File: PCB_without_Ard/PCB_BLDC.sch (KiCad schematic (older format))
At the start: 63 parts, among them J1 Power Terminal, J2 Conn_01x03, J3 Conn_01x05, J4 Conn_01x02, J5 Conn_01x04, J6 Conn_01x04, J7 Conn_01x04, J8 Power Terminal, J9 Conn_01x02, Q1 IRF4905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

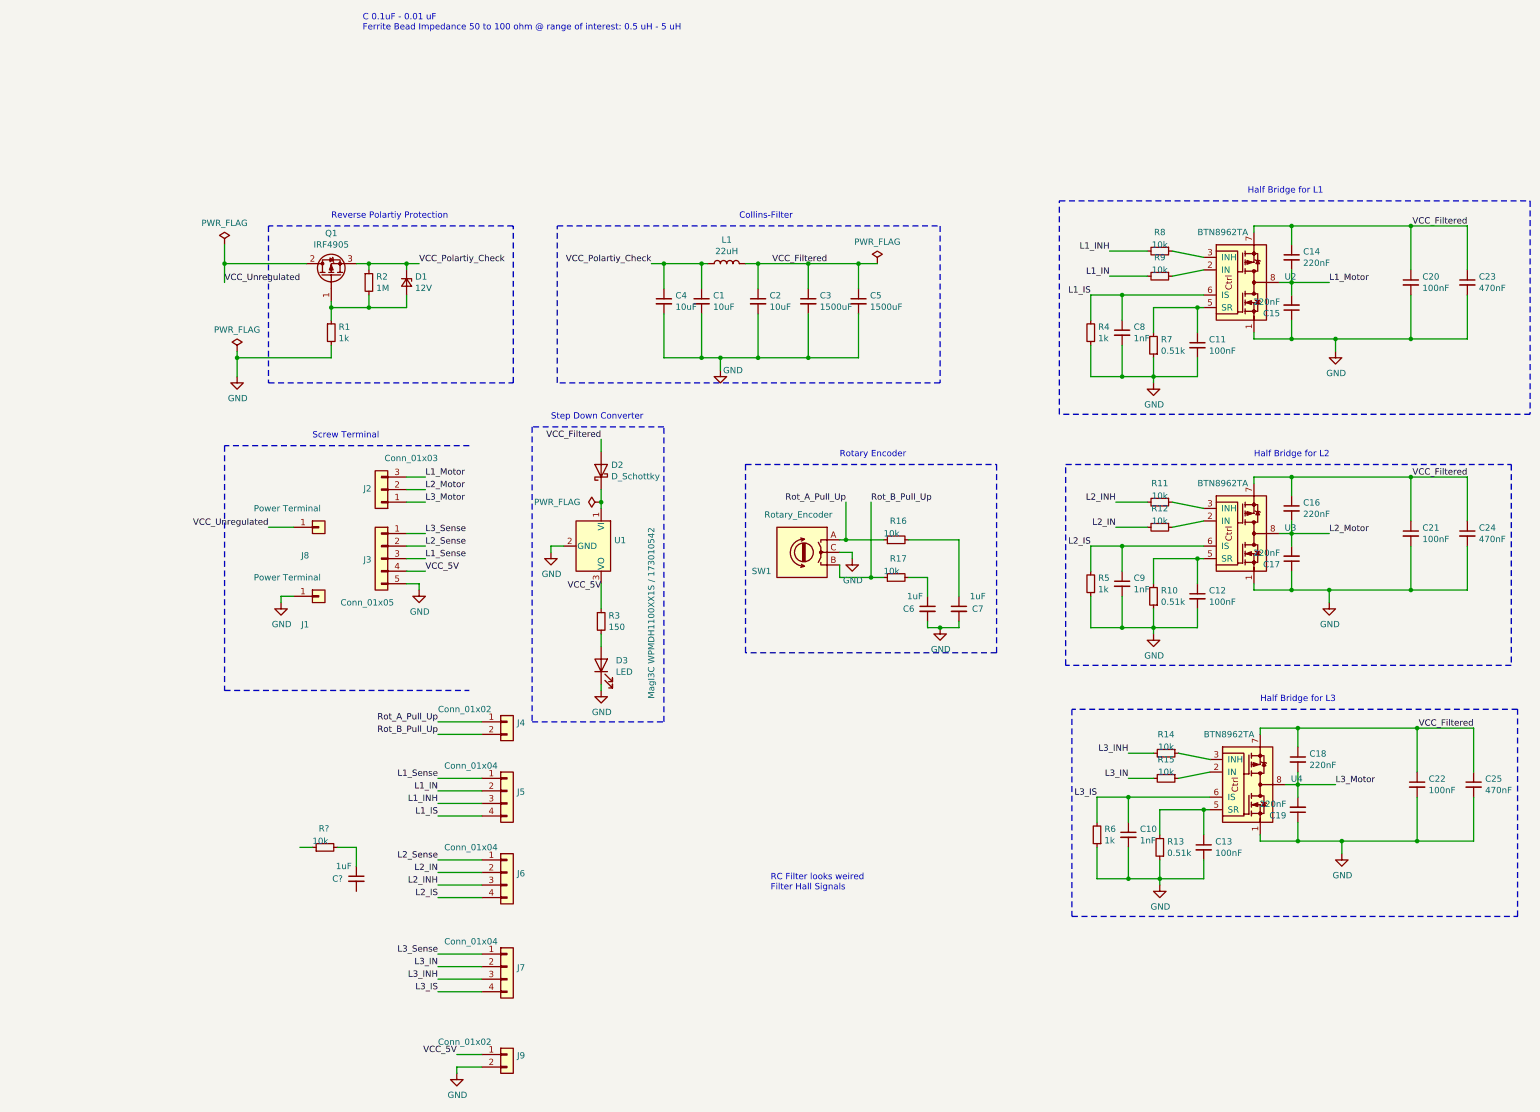
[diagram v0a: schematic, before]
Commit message: Main: Update Schematic, Add Vias, RC-Filt for Hall-Sense
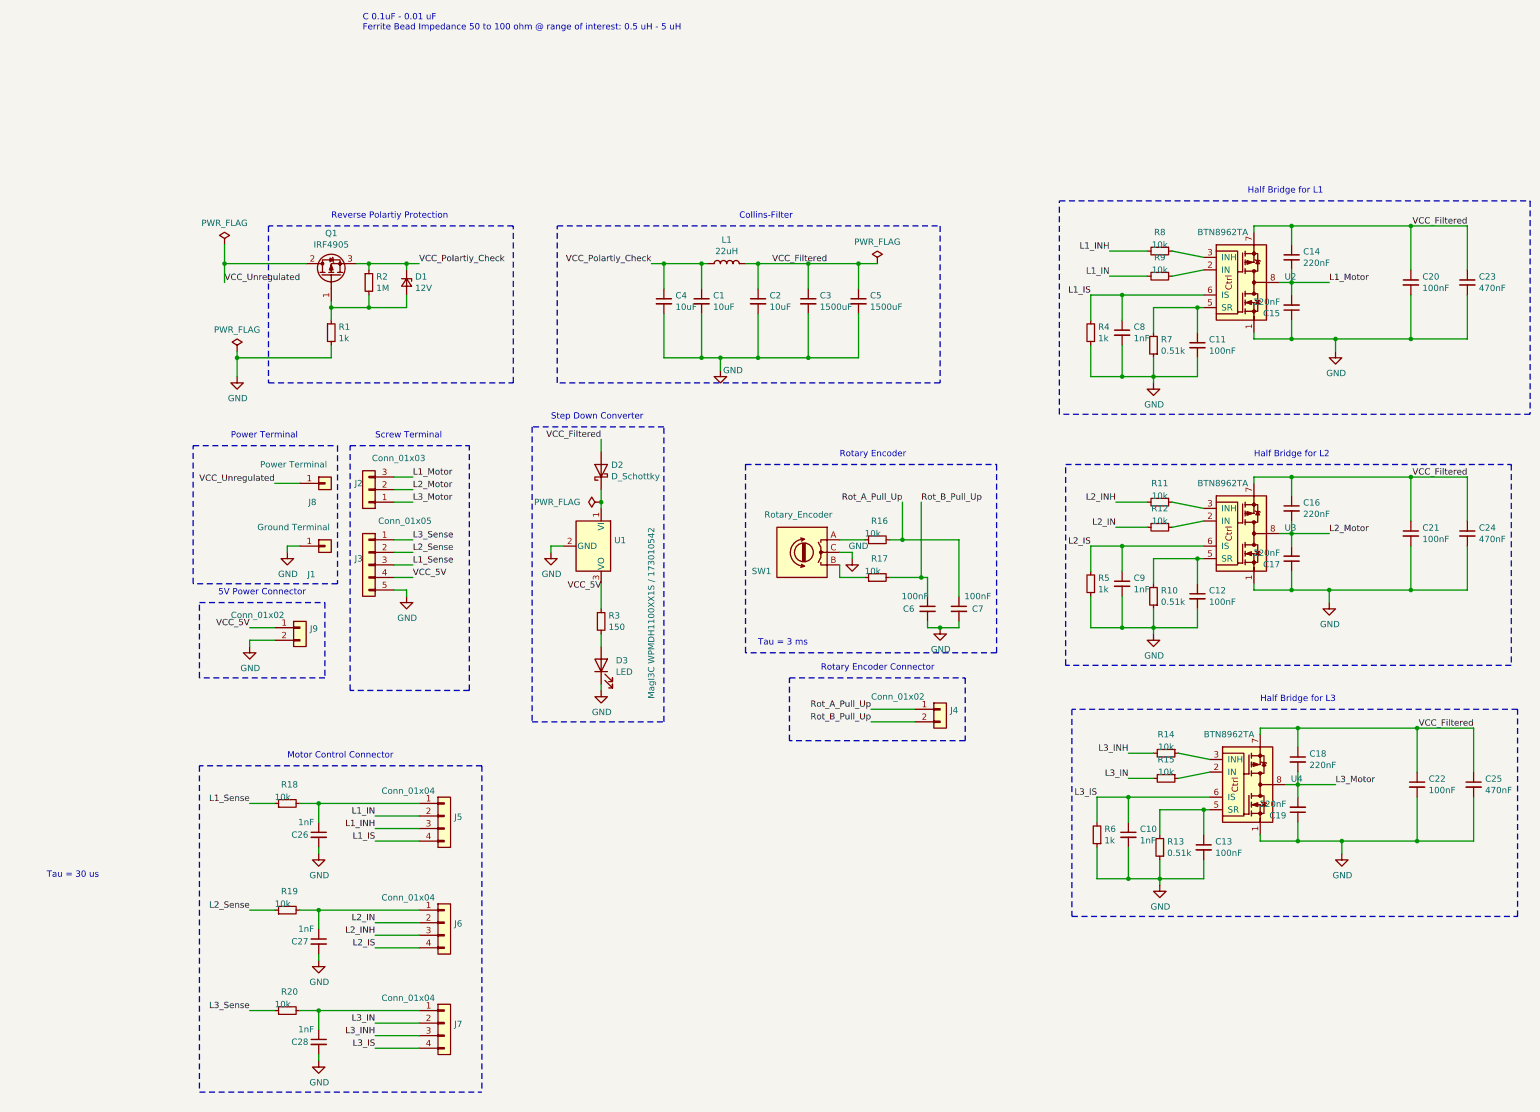
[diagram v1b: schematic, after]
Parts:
- added C27, C28: 1nF, Capacitor_SMD:C_1206_3216Metric_Pad1.33x1.80mm_HandSolder, symbol Device:C_Small
- added R19, R20: 10k, Resistor_SMD:R_1206_3216Metric_Pad1.30x1.75mm_HandSolder, symbol Device:R_Small
- C26: renamed from C?; value 1uF -> 1nF
- C6, C7: value 1uF -> 100nF
- J1: value Power Terminal -> Ground Terminal
- gave numbers to parts that had none: 1
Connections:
- net GND: now also C26.2, C27.2, C28.2
- net L1_Sense: now also R18.1; no longer J5.1 (Pin_1)
- net L2_Sense: now also R19.1; no longer J6.1 (Pin_1)
- net L3_Sense: now also R20.1; no longer J7.1 (Pin_1)
- net Rot_A_Pull_Up: now also C7.1, R16.2; no longer R16.1, SW1.A
- net Rot_B_Pull_Up: now also C6.1, R17.2; no longer R17.1, SW1.B
- net at C26.1, R18.2: now also J5.1 (Pin_1)
- new net: R16.1, SW1.A
- new net: R17.1, SW1.B
- new net: C28.1, J7.1 (Pin_1), R20.2
- new net: C27.1, J6.1 (Pin_1), R19.2
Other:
- note added: "5V Power Connector\n"
- note added: "Motor Control Connector\n"
- note added: "Power Terminal\n"
- note added: "Rotary Encoder Connector\n"
- note added: "Tau = 3 ms"
- note added: "Tau = 30 us"
- note removed: "RC Filter looks weired\nFilter Hall Signals"
- moved on the sheet: C26, J1, J2, J3, J4, J5, J6, J7, J8, J9, R16, R17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

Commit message: PCB: Fixed again Low Pass Filter
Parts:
- added R21, R22, R23, R24, R25: 10k, Resistor_SMD:R_1206_3216Metric_Pad1.30x1.75mm_HandSolder, symbol Device:R_Small
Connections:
- net L1_Sense: now also R21.1
- net L2_Sense: now also R22.1
- net L3_Sense: now also R23.1
- net VCC_5V: now also R21.2, R22.2, R23.2, R24.2, R25.2
- net at R16.1, SW1.A: now also R24.1
- net at R17.1, SW1.B: now also R25.1
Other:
- moved on the sheet: R16, R17
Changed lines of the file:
@@
 Text Label 6300 3050 0    50   ~ 0
 Rot_B_Pull_Up
-Text Label 6150 3050 2    50   ~ 0
+Text Label 6200 2850 0    50   ~ 0
 Rot_A_Pull_Up
 Text Label 10650 850  2    50   ~ 0
@@
 L Device:R_Small R16
 U 1 1 618D47A1
-P 5950 3350
-F 0 "R16" V 6100 3400 50  0000 R CNN
-F 1 "10k" V 6000 3450 50  0000 R CNN
-F 2 "Resistor_SMD:R_1206_3216Metric_Pad1.30x1.75mm_HandSolder" H 5950 3350 50  0001 C CNN
-F 3 "~" H 5950 3350 50  0001 C CNN
-	1    5950 3350
+P 6100 3350
+F 0 "R16" V 6250 3400 50  0000 R CNN
+F 1 "10k" V 6150 3450 50  0000 R CNN
+F 2 "Resistor_SMD:R_1206_3216Metric_Pad1.30x1.75mm_HandSolder" H 6100 3350 50  0001 C CNN
+F 3 "~" H 6100 3350 50  0001 C CNN
+	1    6100 3350
 	0    -1   -1   0
 $EndComp
@@
 L Device:R_Small R17
 U 1 1 618D5B25
-P 5950 3650
-F 0 "R17" V 6100 3700 50  0000 R CNN
-F 1 "10k" V 6000 3750 50  0000 R CNN
-F 2 "Resistor_SMD:R_1206_3216Metric_Pad1.30x1.75mm_HandSolder" H 5950 3650 50  0001 C CNN
-F 3 "~" H 5950 3650 50  0001 C CNN
-	1    5950 3650
+P 6100 3650
+F 0 "R17" V 6250 3700 50  0000 R CNN
+F 1 "10k" V 6150 3750 50  0000 R CNN
+F 2 "Resistor_SMD:R_1206_3216Metric_Pad1.30x1.75mm_HandSolder" H 6100 3650 50  0001 C CNN
+F 3 "~" H 6100 3650 50  0001 C CNN
+	1    6100 3650
 	0    -1   -1   0
 $EndComp
@@
 	5650 3450 5750 3450
 Wire Wire Line
-	6050 3650 6300 3650
+	6200 3650 6300 3650
 Wire Wire Line
 	6350 3650 6350 3800
@@
 	950  4150 950  4200
 Wire Wire Line
-	5650 3650 5850 3650
-Wire Wire Line
-	5650 3350 5850 3350
+	5650 3650 5950 3650
+Wire Wire Line
+	5650 3350 5750 3350
 Wire Wire Line
 	6300 3050 6300 3650
@@
 	6300 3650 6350 3650
 Wire Wire Line
-	6150 3050 6150 3350
-Wire Wire Line
-	6050 3350 6150 3350
-Connection ~ 6150 3350
-Wire Wire Line
-	6150 3350 6600 3350
-Wire Wire Line
 	1350 5450 1500 5450
-Wire Wire Line
-	950  5450 1150 5450
 Wire Wire Line
 	1500 5800 1500 5850
@@
 	1350 7100 1500 7100
 Wire Wire Line
-	950  7100 1150 7100
-Wire Wire Line
 	1500 7450 1500 7500
 $Comp
@@
 Text Label 950  7100 2    50   ~ 0
 L3_Sense
-Wire Wire Line
-	1500 5450 2300 5450
 Connection ~ 1500 5450
-Wire Wire Line
-	1500 7100 2300 7100
 Connection ~ 1500 7100
 Wire Wire Line
 	1350 6300 1500 6300
 Wire Wire Line
-	950  6300 1150 6300
+	950  6300 1050 6300
 Wire Wire Line
 	1500 6650 1500 6700
@@
 	0    -1   -1   0
 $EndComp
-Wire Wire Line
-	1500 6300 2300 6300
 Connection ~ 1500 6300
 Text Notes -250 6050 2    50   ~ 0
@@
 Text Notes 5500 4400 0    50   ~ 0
 Rotary Encoder Connector\n
+$Comp
+L Device:R_Small R24
+U 1 1 618BE346
+P 5750 3100
+F 0 "R24" V 5900 3150 50  0000 R CNN
+F 1 "10k" V 5800 3200 50  0000 R CNN
+F 2 "Resistor_SMD:R_1206_3216Metric_Pad1.30x1.75mm_HandSolder" H 5750 3100 50  0001 C CNN
+F 3 "~" H 5750 3100 50  0001 C CNN
+	1    5750 3100
+	-1   0    0    1
+$EndComp
+Wire Wire Line
+	6200 2850 6200 3350
+Connection ~ 6200 3350
+Wire Wire Line
+	6200 3350 6600 3350
+Wire Wire Line
+	5750 3200 5750 3350
+Connection ~ 5750 3350
+Wire Wire Line
+	5750 3350 6000 3350
+$Comp
+L Device:R_Small R25
+U 1 1 61904EA6
+P 5950 3100
+F 0 "R25" V 6100 3150 50  0000 R CNN
+F 1 "10k" V 6000 3200 50  0000 R CNN
+F 2 "Resistor_SMD:R_1206_3216Metric_Pad1.30x1.75mm_HandSolder" H 5950 3100 50  0001 C CNN
+F 3 "~" H 5950 3100 50  0001 C CNN
+	1    5950 3100
+	-1   0    0    1
+$EndComp
+Wire Wire Line
+	5950 3200 5950 3650
+Connection ~ 5950 3650
+Wire Wire Line
+	5950 3650 6000 3650
+Wire Wire Line
+	5950 3000 5950 2950
+Wire Wire Line
+	5950 2950 5750 2950
+Wire Wire Line
+	5750 2950 5750 3000
+Text Label 5750 2950 2    50   ~ 0
+VCC_5V
+Wire Wire Line
+	1050 6250 1050 6300
+Connection ~ 1050 6300
+Wire Wire Line
+	1050 6300 1150 6300
+Wire Wire Line
+	1500 7100 2300 7100
+Wire Wire Line
+	1050 6800 1050 6850
+Text Label 1050 6800 2    50   ~ 0
+VCC_5V
+$Comp
+L Device:R_Small R23
+U 1 1 61975DAD
+P 1050 6950
+F 0 "R23" V 1200 7000 50  0000 R CNN
+F 1 "10k" V 1100 7050 50  0000 R CNN
+F 2 "Resistor_SMD:R_1206_3216Metric_Pad1.30x1.75mm_HandSolder" H 1050 6950 50  0001 C CNN
+F 3 "~" H 1050 6950 50  0001 C CNN
+	1    1050 6950
+	-1   0    0    1
+$EndComp
+Wire Wire Line
+	1050 7100 1150 7100
+Wire Wire Line
+	950  7100 1050 7100
+Connection ~ 1050 7100
+Wire Wire Line
+	1050 7050 1050 7100
+Wire Wire Line
+	1500 6300 2300 6300
+Text Label 1050 5950 2    50   ~ 0
+VCC_5V
+Wire Wire Line
+	1050 6050 1050 5950
+$Comp
+L Device:R_Small R22
+U 1 1 61952AAA
+P 1050 6150
+F 0 "R22" V 1200 6200 50  0000 R CNN
+F 1 "10k" V 1100 6250 50  0000 R CNN
+F 2 "Resistor_SMD:R_1206_3216Metric_Pad1.30x1.75mm_HandSolder" H 1050 6150 50  0001 C CNN
+F 3 "~" H 1050 6150 50  0001 C CNN
+	1    1050 6150
+	-1   0    0    1
+$EndComp
 Text Notes 1250 5100 0    50   ~ 0
 Motor Control Connector\n
+Text Label 1050 5100 2    50   ~ 0
+VCC_5V
+Wire Wire Line
+	1500 5450 2300 5450
+Wire Wire Line
+	1050 5100 1050 5200
+Wire Wire Line
+	1050 5450 1150 5450
+Wire Wire Line
+	950  5450 1050 5450
+Connection ~ 1050 5450
+Wire Wire Line
+	1050 5400 1050 5450
+$Comp
+L Device:R_Small R21
+U 1 1 6192D640
+P 1050 5300
+F 0 "R21" V 1200 5350 50  0000 R CNN
+F 1 "10k" V 1100 5400 50  0000 R CNN
+F 2 "Resistor_SMD:R_1206_3216Metric_Pad1.30x1.75mm_HandSolder" H 1050 5300 50  0001 C CNN
+F 3 "~" H 1050 5300 50  0001 C CNN
+	1    1050 5300
+	-1   0    0    1
+$EndComp
 $EndSCHEMATC

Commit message: PCB: Changed Power Terminals to correct one, Adapted csv-File to PT1-Filter
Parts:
- J1, J8: footprint Connector:Banana_Jack_1Pin -> Connector:CalTest_CT3151
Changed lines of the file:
@@
 F 0 "J8" H 1450 2750 50  0000 C CNN
 F 1 "Power Terminal" H 1300 3050 50  0000 C CNN
-F 2 "Connector:Banana_Jack_1Pin" H 1550 2900 50  0001 C CNN
+F 2 "Connector:CalTest_CT3151" H 1550 2900 50  0001 C CNN
 F 3 "~" H 1550 2900 50  0001 C CNN
 	1    1550 2900
@@
 F 0 "J1" H 1442 3175 50  0000 C CNN
 F 1 "Ground Terminal" H 1300 3550 50  0000 C CNN
-F 2 "Connector:Banana_Jack_1Pin" H 1550 3400 50  0001 C CNN
+F 2 "Connector:CalTest_CT3151" H 1550 3400 50  0001 C CNN
 F 3 "~" H 1550 3400 50  0001 C CNN
 	1    1550 3400
